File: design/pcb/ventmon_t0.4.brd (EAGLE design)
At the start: 85 x 56 mm, 77 parts, among them IC1 BME280BM280-HAT, J6 Header-16, J7 Header-12, U1 W5500, U2 ADS1115IDGST, Y1 25MHz

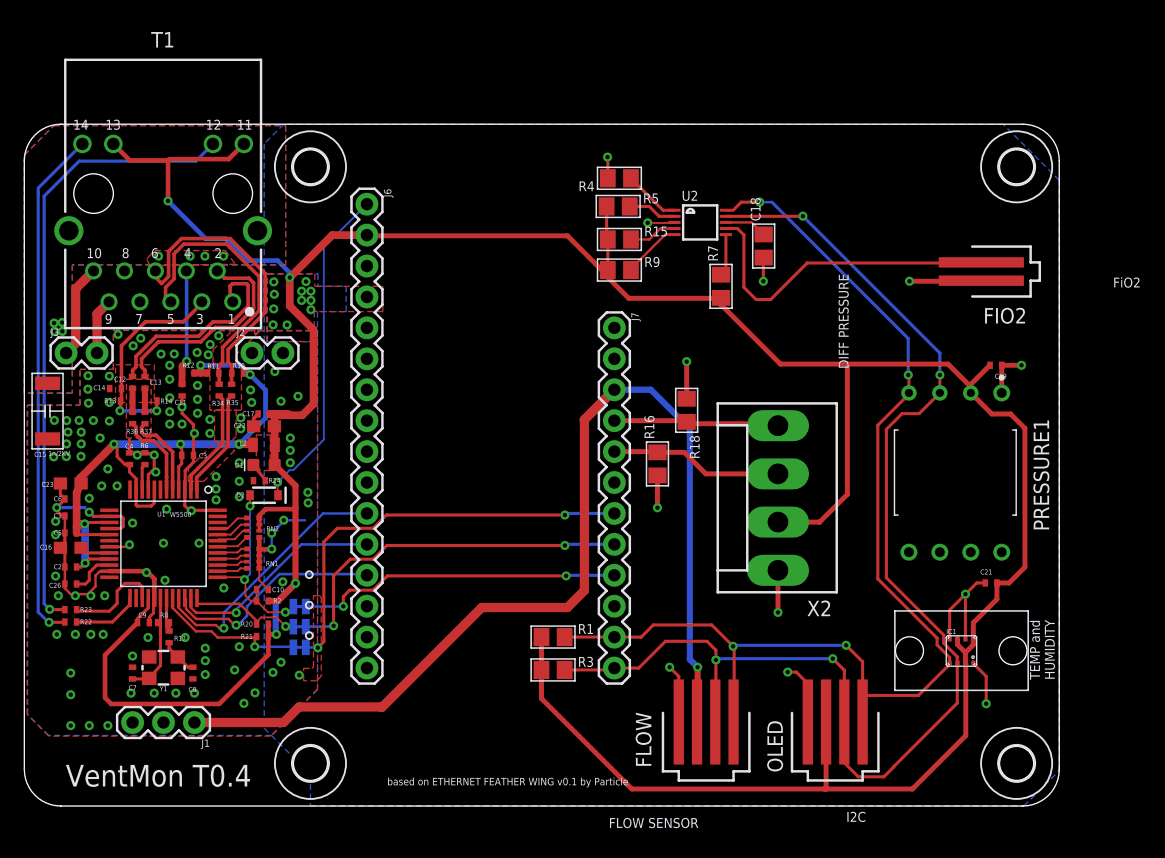
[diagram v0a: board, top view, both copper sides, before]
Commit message: Fixed missing 3v3 wire, added groundplane, fixed DRC errors
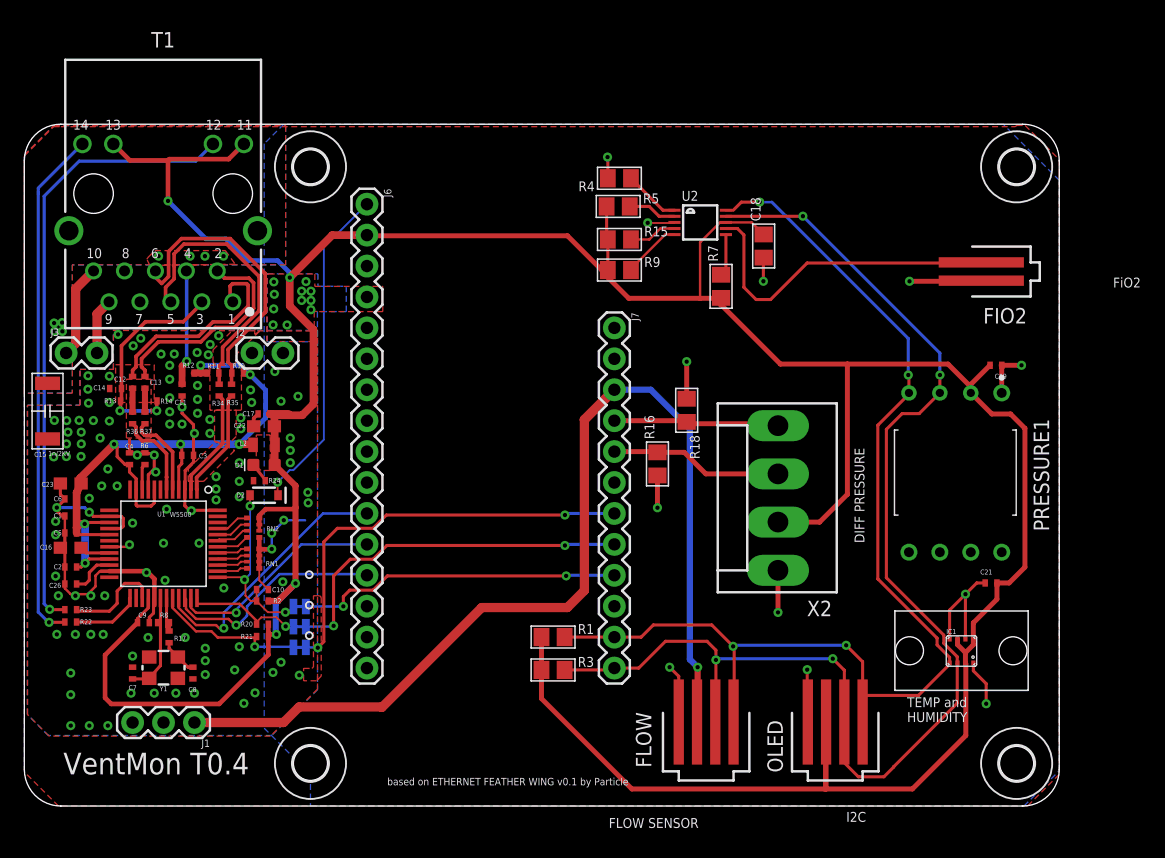
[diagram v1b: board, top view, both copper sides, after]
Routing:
- net +3V3: track 281.3 -> 294.8 mm
- net SDA: track 101.6 -> 106.8 mm
- net SCL: track 93.3 -> 98.0 mm
- net FIO2: track 24.5 -> 27.2 mm
- net +5V: track 84.0 -> 86.0 mm
- net GND: track 109.8 -> 109.0 mm

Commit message: Moved pressure sensors to accomodate small tube
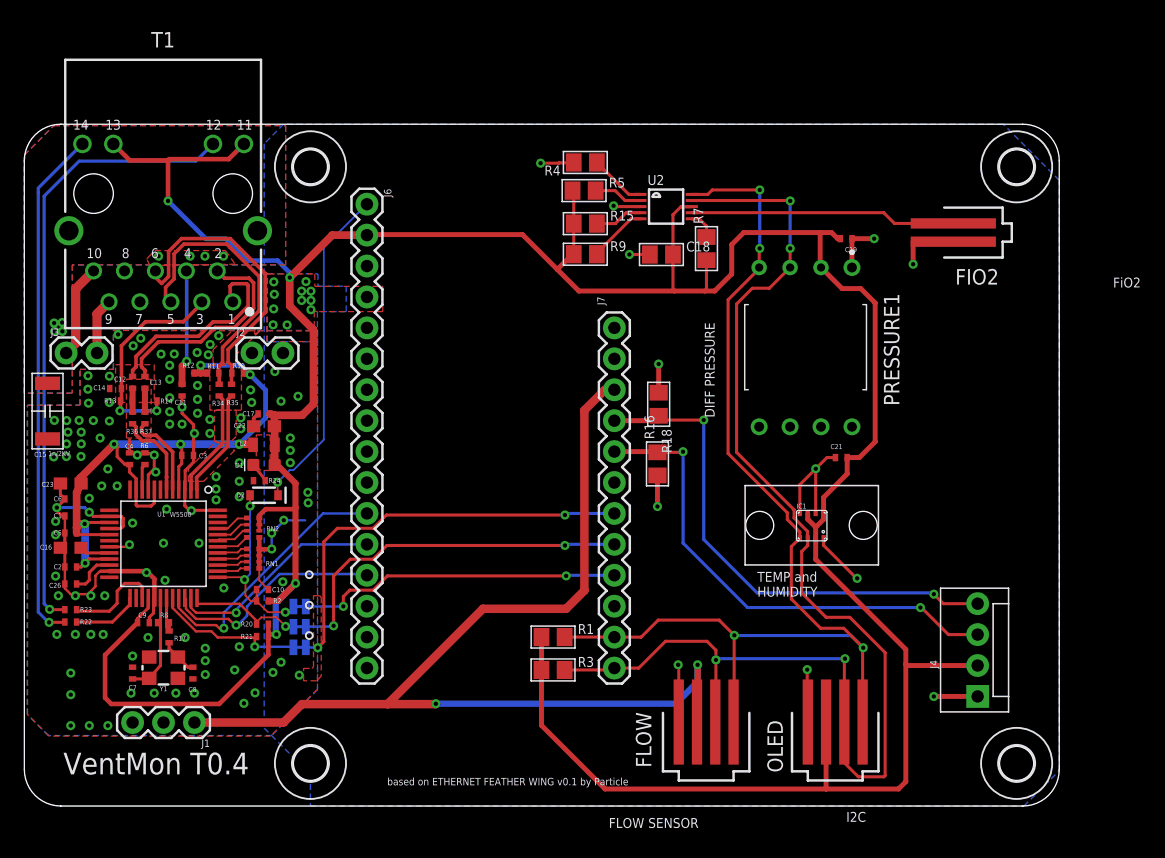
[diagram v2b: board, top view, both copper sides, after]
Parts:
- removed X2: (no value), con-molex:KK-156-4
- added J4: (no value), SparkFun-Connectors:MOLEX-1X4
- moved C19 16.1 mm to (67.5, 46.6)
- moved IC1 16.0 mm to (63.4, 24.3)
- moved C21 16.0 mm to (67.1, 28.6)
- moved PRESSURE1 16.0 mm to (64.2, 37.7)
- moved C18 8.43 mm to (52.3, 45.3), turned to 0 degrees
- moved FIO2 3.94 mm to (76.3, 47.1)
- moved R7 3.32 mm to (56.0, 45.8)
- moved R4 3.09 mm to (46.1, 52.9)
- moved R15 3.09 mm to (46.1, 47.8)
- moved R9 3.09 mm to (46.1, 45.3)
- moved U2 3.09 mm to (52.7, 49.2)
- moved R5 3.09 mm to (46.0, 50.5)
- moved R18 2.35 mm to (52.1, 33.0)
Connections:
- net +3V3: now also J4.2; no longer X2.2
- net BTNA: now also J4.4; no longer X2.4
- net BTNB: now also J4.3; no longer X2.3
- net GND: now also J4.1; no longer X2.1
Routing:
- net BTNA: track 13.8 -> 42.3 mm, vias 0 -> 2
- net BTNB: track 14.2 -> 40.5 mm, vias 0 -> 2
- net +3V3: track 294.8 -> 277.9 mm
- net SCL: track 98.0 -> 90.0 mm
- net FIO2: track 27.2 -> 21.8 mm
- net GND: track 109.0 -> 112.1 mm
- net N$38: track 3.46 -> 2.35 mm
- net +5V: track 86.0 -> 86.8 mm, vias 1 -> 2
